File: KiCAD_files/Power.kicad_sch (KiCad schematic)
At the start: 63 parts, among them J101 2604-1102, J102 2604-1102, J103 2604-1102, J104 Conn_01x01, J105 Conn_01x01, J106 Conn_01x01, J107 Conn_01x01, J108 Conn_01x01, J109 Conn_01x01, J110 Conn_01x01, J111 Conn_01x01, J112 Conn_01x01, J113 Conn_01x01, J114 Conn_01x01, J115 Conn_01x01, J116 Conn_01x01, J117 2604-1102, J118 2604-1102, U101 AMC1311, U102 OPA316, U103 OPA316, U104 +-20A

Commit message: Supressed backup files
Former-commit-id: af6064aba0445a9773bde6e74b771947025d2895
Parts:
- added H1, H2, H3, H4, H5, H6: MountingHole, MountingHole:MountingHole_3.2mm_M3, symbol Mechanical:MountingHole
- added Rbleed1, Rbleed2: 1M, Resistor_SMD:R_0805_2012Metric, symbol Device:R_Small
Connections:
- net GNDREF: now also Rbleed2.2
- net VI_High: no longer J113.1 (Pin_1)
- net V_High: now also J113.1 (Pin_1), Rbleed1.1
- net at C111.2, C112.1, C113.2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: no longer C105.2, C106.1, C107.2, C108.1, C109.2, C110.1
- new net: C105.2, C106.1, C107.2, C108.1, C109.2, C110.1, Rbleed1.2, Rbleed2.1
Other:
- moved on the sheet: C105, C106, C107, C108, C109, C110

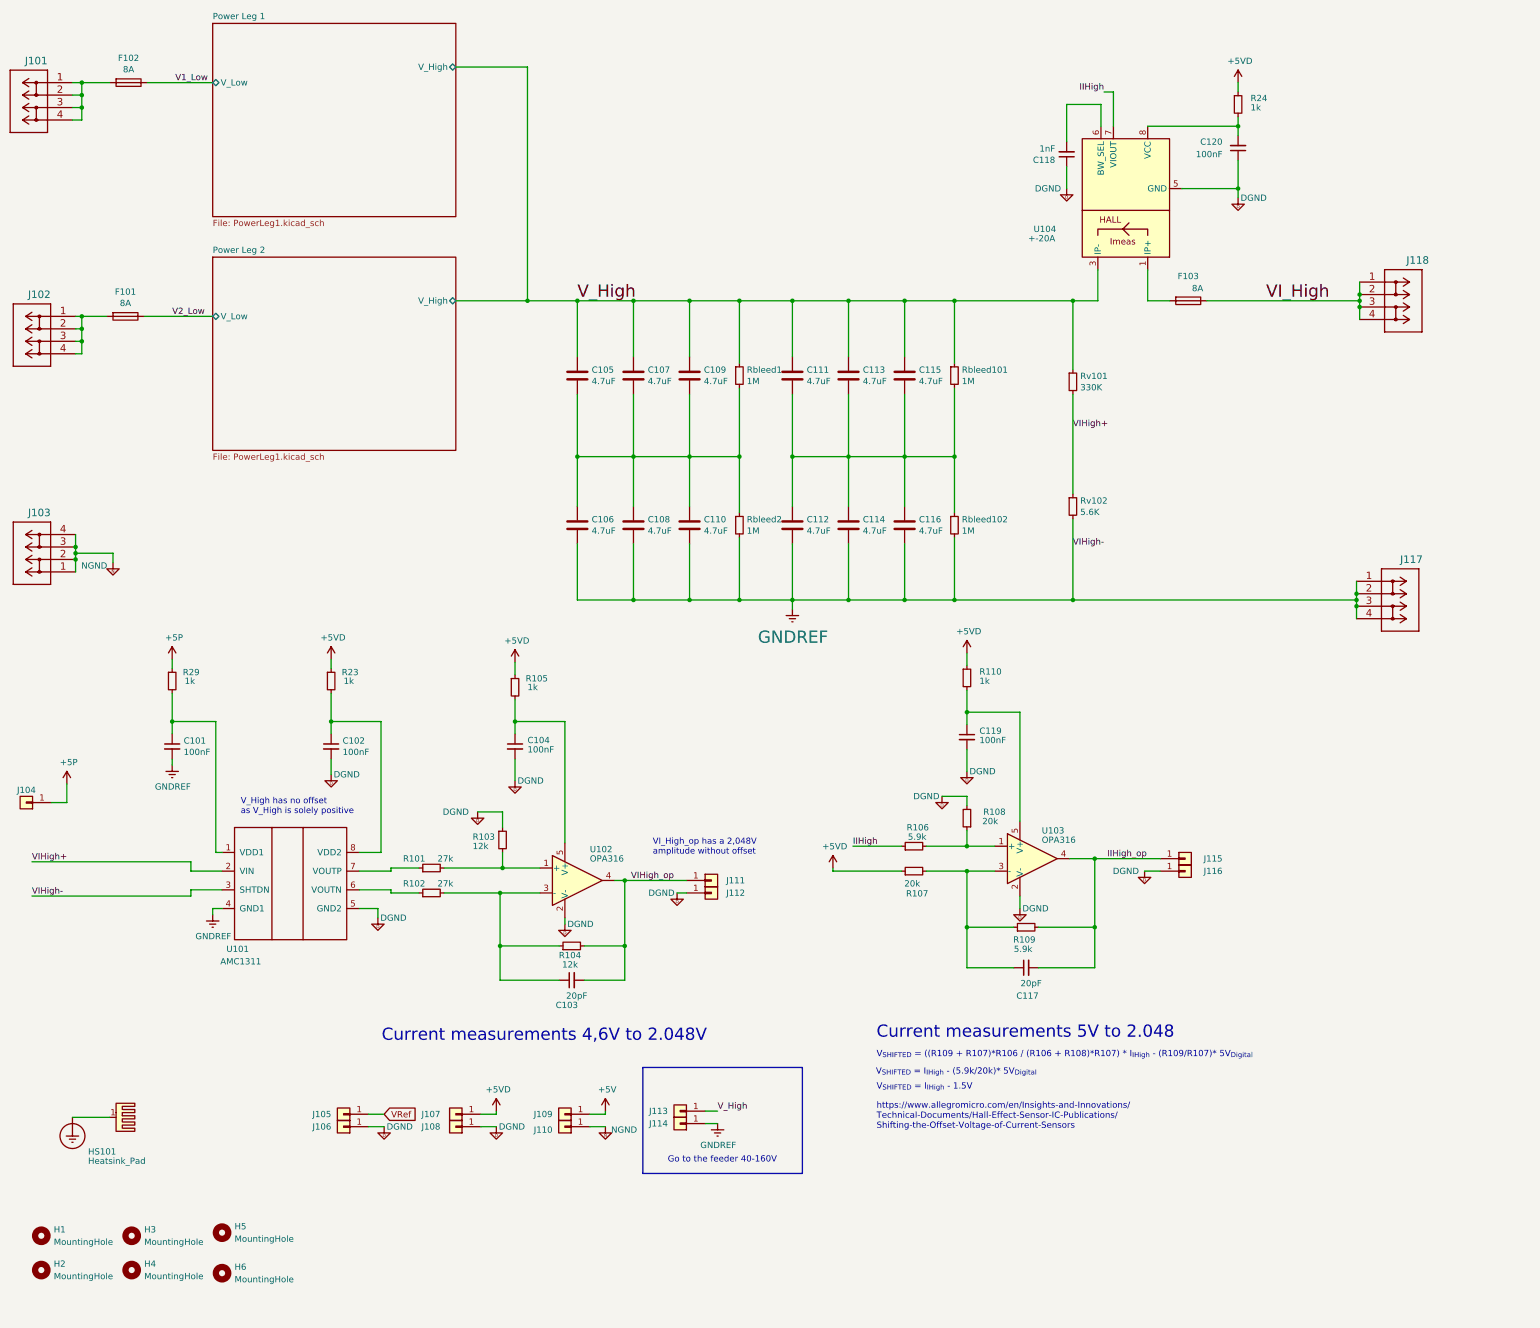
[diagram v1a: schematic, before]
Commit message: WIP: mooving to a single board implementation with 160x100 form factor.
Former-commit-id: e8c19d5fc5237412fb5a003591d44756dbc6e173
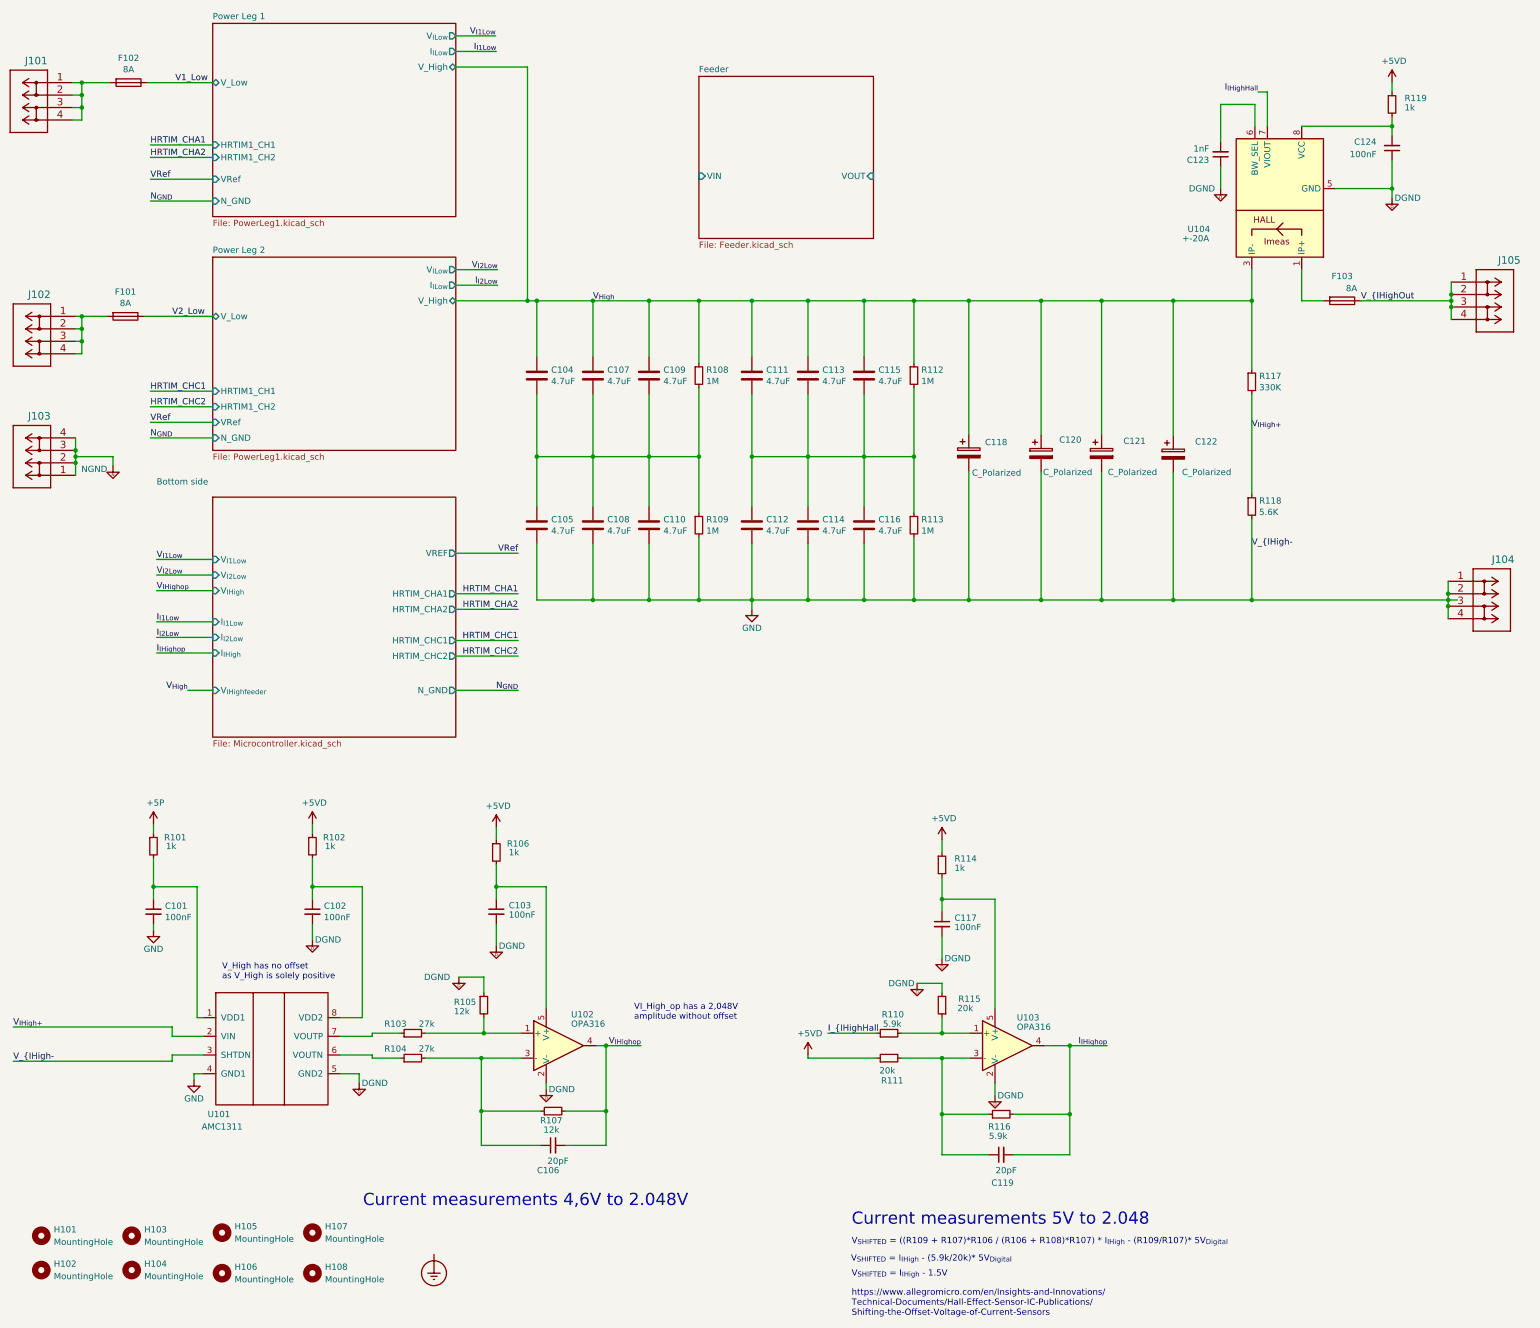
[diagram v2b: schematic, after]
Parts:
- removed HS101: Heatsink_Pad, Footprints:custom_heatsink, symbol Mechanical:Heatsink_Pad
- removed J104, J105, J106, J107, J108, J109, J110, J111, J112, J113, J114, J115, J116: Conn_01x01, Footprints:0906_millmax, symbol Connector_Generic:Conn_01x01
- added C118, C120, C121, C122: C_Polarized, Capacitor_SMD:CP_Elec_10x10.5, symbol Device:C_Polarized
- added H107, H108: MountingHole, MountingHole:MountingHole_3.2mm_M3, symbol Mechanical:MountingHole
- renumbered C104 to C103, C105 to C104, C106 to C105, C103 to C106, C119 to C117, C117 to C119, C118 to C123, C120 to C124, H1 to H101, H2 to H102, H3 to H103, H4 to H104, H5 to H105, H6 to H106, J117 to J104, J118 to J105, R29 to R101, R23 to R102, R101 to R103, R102 to R104, R103 to R105, R105 to R106, R104 to R107, Rbleed1 to R108, Rbleed2 to R109, R106 to R110, R107 to R111, Rbleed101 to R112, Rbleed102 to R113, R110 to R114, R108 to R115, R109 to R116, Rv101 to R117, Rv102 to R118, R24 to R119
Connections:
- net GNDREF renamed GND
- net GND: now also C118.2, C120.2, C121.2, C122.2
- net IIHigh renamed I_{IHighHall
- net I_{IHighHall: no longer U104.7 (VIOUT)
- net IIHigh_op renamed I_{IHighop}
- net VIHigh+ renamed V_{IHigh+}
- net VIHigh_op renamed V_{IHighop}
- net VI_High renamed V_{IHighOut
- net V_High renamed V_{High}
- net V_{High}: now also C118.1, C120.1, C121.1, C122.1
- new net I_{IHighHall}: U104.7 (VIOUT)
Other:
- added sheet Bottom side (Microcontroller.kicad_sch)
- added sheet Feeder (Feeder.kicad_sch)
- sheet Power Leg 1 ports: added HRTIM1_CH1, HRTIM1_CH2, I_{ILow}, N_GND, VRef, V_{ILow}; removed none
- sheet Power Leg 2 ports: added HRTIM1_CH1, HRTIM1_CH2, I_{ILow}, N_GND, VRef, V_{ILow}; removed none
- note removed: "Go to the feeder 40-160V"
- moved on the sheet: C101, C102, C103, C104, C105, C106, C107, C108, C109, C110, C111, C112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

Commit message: WIP: integrated the feeder on the power board directly
Former-commit-id: e81265b44c994f7ae6e14a178f616f328de7a2ab
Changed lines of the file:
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@@
     (stroke (width 0) (type default) (color 0 0 0 0))
   )
+  (wire (pts (xy 162.56 48.895) (xy 162.56 74.295))
+    (stroke (width 0) (type default) (color 0 0 0 0))
+  )
   (wire (pts (xy 62.23 130.175) (xy 73.66 130.175))
     (stroke (width 0) (type default) (color 0 0 0 0))
@@
     (stroke (width 0) (type default) (color 0 0 0 0))
   )
+  (wire (pts (xy 172.72 48.895) (xy 162.56 48.895))
+    (stroke (width 0) (type default) (color 0 0 0 0))
+  )
   (wire (pts (xy 106.172 227.965) (xy 106.172 228.6))
     (stroke (width 0) (type default) (color 0 0 0 0))
@@
       (reference "#PWR0121") (unit 1) (value "DGND") (footprint "")
     )
+    (path "/122c01f4-f23e-4db0-9503-7261d96dc78b/95c15fce-fd3d-454d-b54f-d07f917e99fc"
+      (reference "#PWR0122") (unit 1) (value "+6V") (footprint "")
+    )
+    (path "/bce1534c-362e-45ed-a9dd-a44d6954485a/533c0480-f16d-4498-a645-5c8cb1931dac"
+      (reference "#PWR0123") (unit 1) (value "DGND") (footprint "")
+    )
+    (path "/bce1534c-362e-45ed-a9dd-a44d6954485a/7b2bd248-b120-49e4-99f0-e5e512ebc4b6"
+      (reference "#PWR0124") (unit 1) (value "+6V") (footprint "")
+    )
+    (path "/122c01f4-f23e-4db0-9503-7261d96dc78b/4f5a6962-7517-458c-8ddb-c795c386772e"
+      (reference "#PWR0125") (unit 1) (value "+5VD") (footprint "")
+    )
+    (path "/122c01f4-f23e-4db0-9503-7261d96dc78b/d02fea88-b4c6-430e-bed0-4423b555c9ad"
+      (reference "#PWR0126") (unit 1) (value "+6V") (footprint "")
+    )
+    (path "/122c01f4-f23e-4db0-9503-7261d96dc78b/95f1c592-e591-4cd3-ad00-0bc57ce37f22"
+      (reference "#PWR0127") (unit 1) (value "DGND") (footprint "")
+    )
     (path "/b9592210-62fd-48e0-8447-67f645d7d247/44457cf5-1c19-4277-9bae-1a0529e9ddd8"
       (reference "#PWR0201") (unit 1) (value "NGND") (footprint "")
@@
       (reference "#PWR0418") (unit 1) (value "DGND") (footprint "")
     )
-    (path "/122c01f4-f23e-4db0-9503-7261d96dc78b/4205ee94-fc3f-4c49-a14d-6d4a3b497b7f"
-      (reference "#PWR0419") (unit 1) (value "GND") (footprint "")
-    )
     (path "/122c01f4-f23e-4db0-9503-7261d96dc78b/00000000-0000-0000-0000-0000627a9ec5"
       (reference "#PWR0420") (unit 1) (value "+3.3V") (footprint "")
@@
       (reference "#PWR0433") (unit 1) (value "+5P") (footprint "")
     )
-    (path "/122c01f4-f23e-4db0-9503-7261d96dc78b/00000000-0000-0000-0000-0000608f259a"
-      (reference "#PWR0434") (unit 1) (value "+5VD") (footprint "")
-    )
-    (path "/122c01f4-f23e-4db0-9503-7261d96dc78b/505e0441-3196-4286-987f-662ad410d867"
-      (reference "#PWR0435") (unit 1) (value "DGND") (footprint "")
-    )
     (path "/122c01f4-f23e-4db0-9503-7261d96dc78b/694ed026-2972-4522-bf54-3804b7935a0e"
       (reference "#PWR0436") (unit 1) (value "DGND") (footprint "")
@@
       (reference "C403") (unit 1) (value "10uF") (footprint "Capacitor_SMD:C_1210_3225Metric")
     )
-    (path "/122c01f4-f23e-4db0-9503-7261d96dc78b/e3c0bb78-4fa3-4a22-b80a-7d9b8b159a66"
-      (reference "C404") (unit 1) (value "4.7u") (footprint "Capacitor_SMD:C_1210_3225Metric")
+    (path "/122c01f4-f23e-4db0-9503-7261d96dc78b/bbeab6cd-2853-4636-8822-3556d8ded29f"
+      (reference "C404") (unit 1) (value "1µF") (footprint "Capacitor_SMD:C_0805_2012Metric")
     )
-    (path "/122c01f4-f23e-4db0-9503-7261d96dc78b/c55397f5-033e-4d8e-8b3d-abaf2f69506e"
-      (reference "C405") (unit 1) (value "4.7u") (footprint "Capacitor_SMD:C_1210_3225Metric")
+    (path "/122c01f4-f23e-4db0-9503-7261d96dc78b/7b8cac1d-fb63-4838-8477-70e30223d257"
+      (reference "C405") (unit 1) (value "1µF") (footprint "Capacitor_SMD:C_0805_2012Metric")
     )
     (path "/122c01f4-f23e-4db0-9503-7261d96dc78b/00000000-0000-0000-0000-000061049c35"
@@
       (reference "C409") (unit 1) (value "1µF") (footprint "Capacitor_SMD:C_0805_2012Metric")
     )
-    (path "/122c01f4-f23e-4db0-9503-7261d96dc78b/b32a35c1-c000-411a-b45e-87b4be51e5f4"
-      (reference "C410") (unit 1) (value "C_Polarized_Small") (footprint "Capacitor_SMD:CP_Elec_10x10.5")
-    )
     (path "/bce1534c-362e-45ed-a9dd-a44d6954485a/f15f9afb-f1b2-4cf2-a355-0d7cbc2f1fc1"
       (reference "C501") (unit 1) (value "4.7uF") (footprint "Capacitor_SMD:C_1210_3225Metric")
@@
       (reference "C516") (unit 1) (value "6.8nF") (footprint "Capacitor_SMD:C_0805_2012Metric")
     )
+    (path "/bce1534c-362e-45ed-a9dd-a44d6954485a/c39d3283-d31f-4644-a33a-4a795f669fa0"
+      (reference "C517") (unit 1) (value "4.7uF") (footprint "Capacitor_SMD:C_1210_3225Metric")
+    )
+    (path "/bce1534c-362e-45ed-a9dd-a44d6954485a/952ca2d4-496f-4590-bc94-923c04914850"
+      (reference "C518") (unit 1) (value "4.7uF") (footprint "Capacitor_SMD:C_1210_3225Metric")
+    )
+    (path "/bce1534c-362e-45ed-a9dd-a44d6954485a/c4789625-151d-4665-9a06-366f4cc9d1d4"
+      (reference "C519") (unit 1) (value "470nF") (footprint "Capacitor_SMD:C_1210_3225Metric")
+    )
+    (path "/bce1534c-362e-45ed-a9dd-a44d6954485a/dc760799-0eb5-425a-9276-d1f9d272c94a"
+      (reference "C520") (unit 1) (value "470nF") (footprint "Capacitor_SMD:C_1210_3225Metric")
+    )
+    (path "/bce1534c-362e-45ed-a9dd-a44d6954485a/8140d103-934b-4677-82ce-bd60f0b69219"
+      (reference "C521") (unit 1) (value "C_Polarized_Small") (footprint "Capacitor_SMD:CP_Elec_10x10.5")
+    )
     (path "/b9592210-62fd-48e0-8447-67f645d7d247/7db2a4b9-f872-48cc-a2a7-1f09e20dda1e"
       (reference "D201") (unit 1) (value "STTH4R02U") (footprint "Diode_SMD:D_SMB")
@@
       (reference "JP404") (unit 1) (value "Jumper") (footprint "Connector_PinHeader_2.54mm:PinHeader_1x02_P2.54mm_Vertical")
     )
-    (path "/122c01f4-f23e-4db0-9503-7261d96dc78b/00000000-0000-0000-0000-00006103a946"
-      (reference "JP405") (unit 1) (value "Jumper") (footprint "Connector_PinHeader_2.54mm:PinHeader_1x02_P2.54mm_Vertical")
+    (path "/bce1534c-362e-45ed-a9dd-a44d6954485a/a031fa4d-af41-4f97-96ec-784a8126bded"
+      (reference "JP501") (unit 1) (value "Jumper") (footprint "Connector_PinHeader_2.54mm:PinHeader_1x02_P2.54mm_Vertical")
     )
     (path "/b9592210-62fd-48e0-8447-67f645d7d247/1e73c20c-5640-4395-9839-e6b19afb1273"
@@
       (reference "L301") (unit 1) (value "33uH") (footprint "Footprints:SRP1510CA-330M")
     )
-    (path "/122c01f4-f23e-4db0-9503-7261d96dc78b/73033138-3f50-48c1-8d76-8f08b271ec11"
-      (reference "L401") (unit 1) (value "L_Small") (footprint "")
-    )
     (path "/bce1534c-362e-45ed-a9dd-a44d6954485a/06062d90-90c4-467e-9d3a-0af9b2872b16"
       (reference "L501") (unit 1) (value "100uH") (footprint "Inductor_SMD:L_0805_2012Metric")
     )
+    (path "/bce1534c-362e-45ed-a9dd-a44d6954485a/9ddf2f31-c80b-4406-95a7-525f60c81c9f"
+      (reference "L502") (unit 1) (value "L") (footprint "")
+    )
     (path "/bce1534c-362e-45ed-a9dd-a44d6954485a/4a824da0-f9ae-4473-ac1b-26c1a66c28a2"
       (reference "NTC501") (unit 1) (value "100k") (footprint "Resistor_SMD:R_0805_2012Metric")
@@
       (reference "PS402") (unit 1) (value "MEE1S0512SC") (footprint "Footprints:Converter_DCDC_Murata_MEE1SxxxxSC_THT")
     )
-    (path "/122c01f4-f23e-4db0-9503-7261d96dc78b/00000000-0000-0000-0000-0000606519f4"
-      (reference "PS403") (unit 1) (value "Feeder") (footprint "Footprints:Feeder")
-    )
     (path "/b9592210-62fd-48e0-8447-67f645d7d247/8b19c1d3-9a78-4e3a-90b2-4dc455c9cbba"
       (reference "Q201") (unit 1) (value "IPD200N15N3") (footprint "Package_TO_SOT_SMD:TO-252-2")
@@
       (reference "U403") (unit 1) (value "MCP1799T-5002H/TT") (footprint "Package_TO_SOT_SMD:SOT-23")
     )
+    (path "/122c01f4-f23e-4db0-9503-7261d96dc78b/1a6e8028-eacb-4254-857e-9b0d8115f6b6"
+      (reference "U404") (unit 1) (value "AP1117-50") (footprint "Package_TO_SOT_SMD:SOT-223-3_TabPin2")
+    )
     (path "/bce1534c-362e-45ed-a9dd-a44d6954485a/99ad4273-f643-44c1-b5af-850a553fee20"

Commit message: WIP : 99 percents of the nets are now routed properly
Former-commit-id: fcbb95e3f0a6512a63faba729c3990d7109d7768
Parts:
- added H109: MountingHole, MountingHole:MountingHole_2.7mm_M2.5, symbol Mechanical:MountingHole
- H101, H102, H103, H104, H105, H106, H107, H108: footprint MountingHole:MountingHole_3.2mm_M3 -> MountingHole:MountingHole_2.7mm_M2.5

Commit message: WIP : Mechanical drawings and fab drawings have been cleaned up
Former-commit-id: 134f220442ec2a3fea5dbd7da82e3ae2ef008ff9
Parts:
- C104, C105, C107, C108, C109, C110, C111, C112, C113, C114, C115, C116: VRating (none) -> 100V
- C118, C120, C121, C122: value C_Polarized -> 33uF; VRating (none) -> 160V
- H101, H102, H103, H104, H105, H106, H107, H108, H109: value MountingHole -> M2.5
